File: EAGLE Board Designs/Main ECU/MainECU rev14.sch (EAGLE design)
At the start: 319 parts, among them J1 CONNECTOR-34__, J2 CONNECTOR-34__, J3 ADIS16460, K1 RELAY_DPDT_07DSMT, K2 RELAY_DPDT_07DSMT, K3 RELAY_DPDT_07DSMT, K4 RELAY_DPDT_07DSMT, K5 RELAY_DPDT_07DSMT, Q1 TRANSISTOR_N_MOS__DMG3406L-7, Q2 TRANSISTOR_P_MOS_SOT-23_DMP30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, Q3 TRANSISTOR_P_MOS_SOT-23_DMP30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, Q4 TRANSISTOR_N_MOS__DMG3406L-7, U1 MAX7400, U10 MCP3208, U11 MCP3208, U12 TCAN1051HQV-Q1, U13 TCAN1051HQV-Q1, U15 OPAMP_1_CHANNEL_OPA991, U16 LOGICGATE_OR, U17 OPAMP_1_CHANNEL_OPA991, U18 LOGICGATE_OR, U19 OPAMP_1_CHANNEL_OPA991, U2 MAX7400, U20 LOGICGATE_OR, U21 LOGICGATE_OR, U22 OPAMP_1_CHANNEL_OPA991, U23 LOGICGATE_NOR, U24 LOGICGATE_OR, U25 OPAMP_1_CHANNEL_OPA991, U26 OPAMP_1_CHANNEL_OPA991, U27 OPAMP_1_CHANNEL_OPA991, U28 LOGICGATE_AND_DCK3, U29 OPAMP_1_CHANNEL_OPA991, U3 MAX7400, U30 OPAMP_1_CHANNEL_OPA991, U31 TCAN1051HQV-Q1, U32 TCAN1051HQV-Q1, U33 TCAN1051HQV-Q1, U34 TCAN1051HQV-Q1, U35 MAX7400, U36 MAX7400, U37 ADM8316WBX30, U38 MAX7400, U4 MAX7400, U5 VOLTAGE_REGULATOR_SOT-223_3.3V, U6 MAX7400, U7 MAX7400, U8 MAX7400, U9 MAX7400

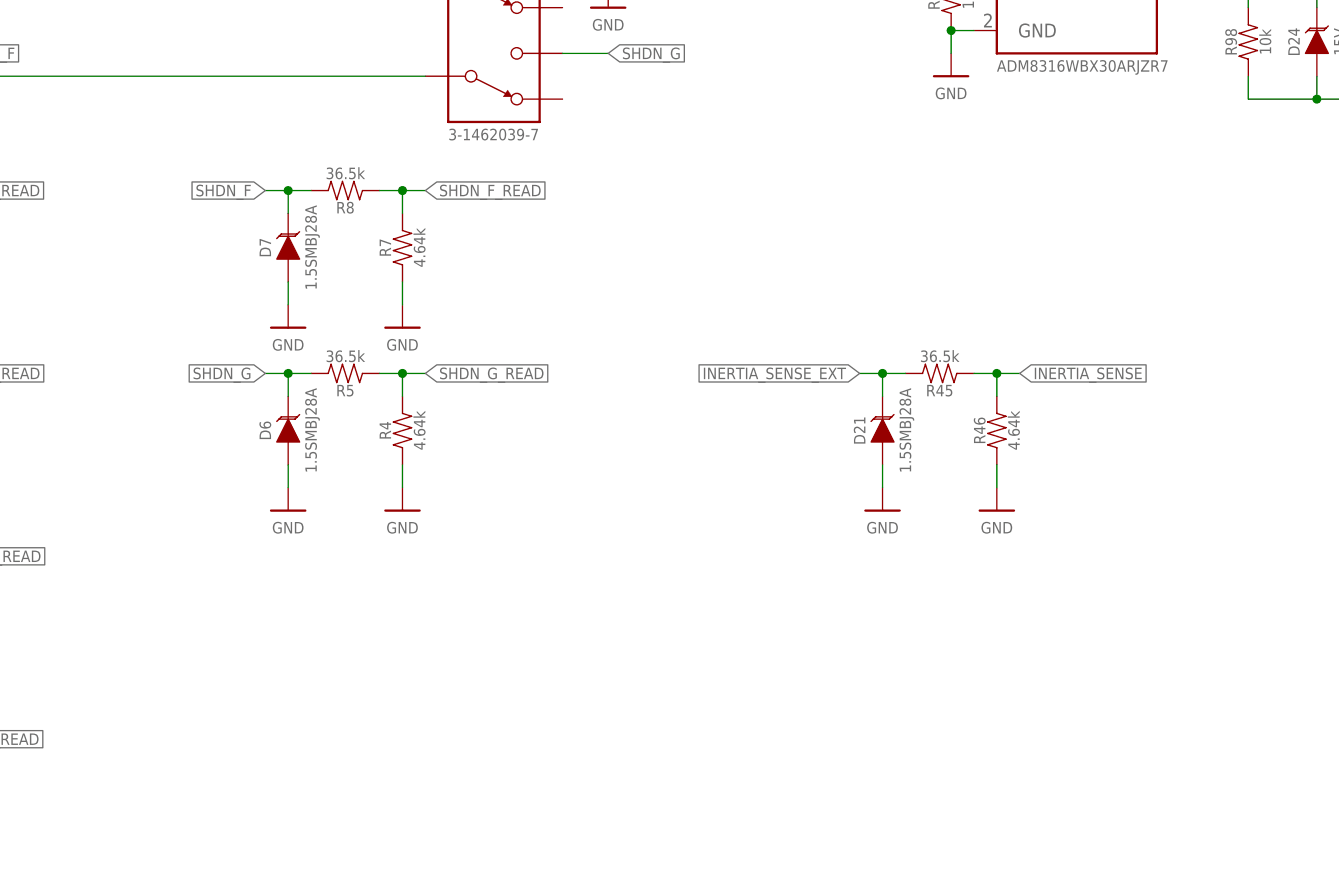
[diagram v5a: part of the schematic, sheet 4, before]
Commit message: added ECU->TCU serial, AMS&IMD sense
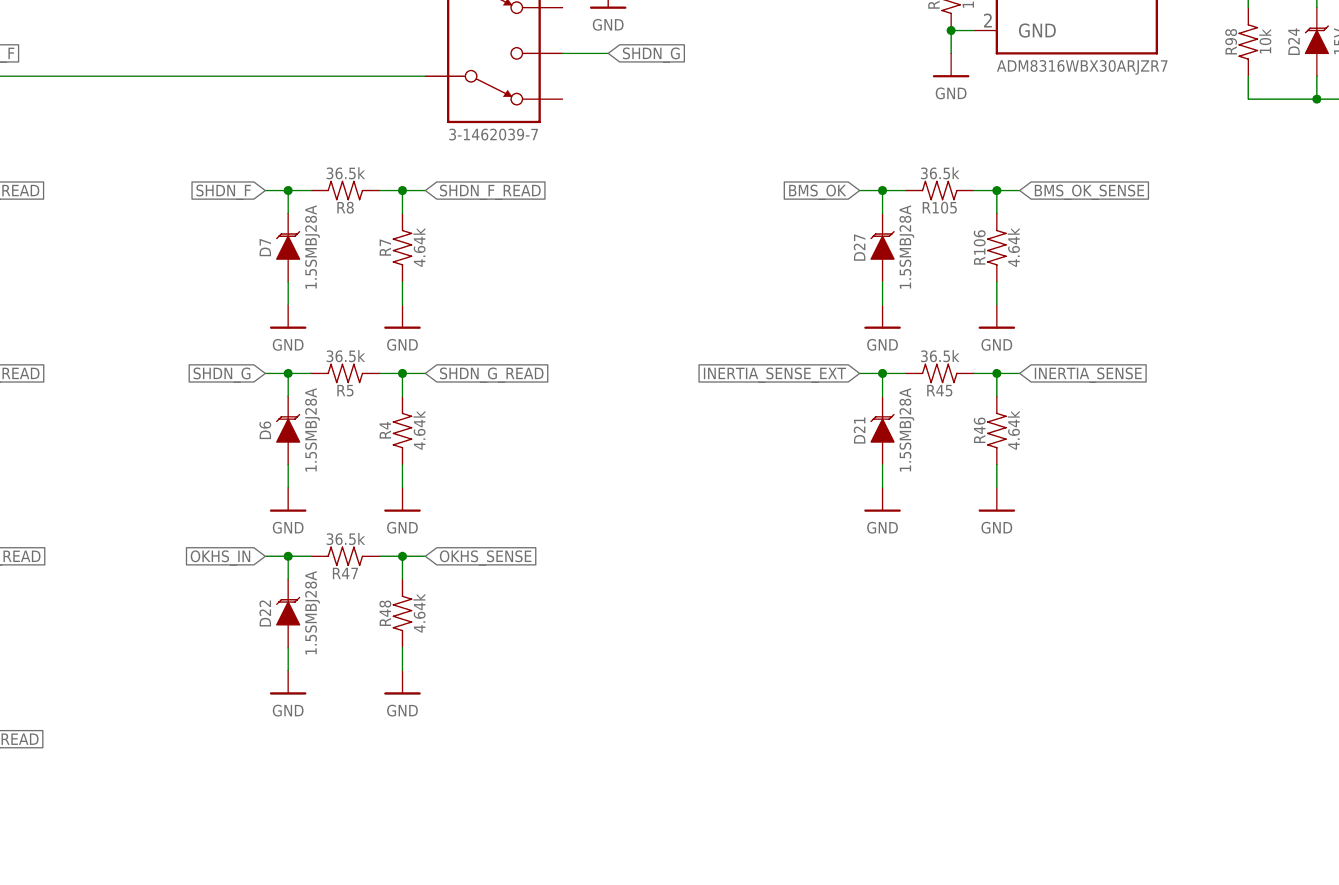
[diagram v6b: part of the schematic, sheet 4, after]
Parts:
- added D22, D27: TVS_DO-214AA_28V, HyTechDevices:TVS_DO-214AA_28V
- added R105, R47: RESISTOR_0603_36.5K, HyTechDevices:RESISTOR_0603_36.5K
- added R106, R48: RESISTOR_0603_4.64K, HyTechDevices:RESISTOR_0603_4.64K
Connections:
- removed net GPS_RX: A3.A0
- removed net GPS_TX: A3.A1
- new net BMS_OK_SENSE: A2.A2, R105.1, R106.2
- new net ECU_RX3: A2.A1, A3.A0
- new net ECU_TX3: A2.A0, A3.A1
- new net OKHS_SENSE: A2.A4, R47.1, R48.2
- net BMS_OK: now also D27.C, R105.2
- net GND: now also D22.A, D27.A, R106.1, R48.1
- net OKHS_IN: now also D22.C, R47.2
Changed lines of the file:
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@@
 <part name="P57" library="HyTechSupplies" deviceset="+3V3" device=""/>
 <part name="P58" library="HyTechSupplies" deviceset="+3V3" device=""/>
+<part name="R47" library="HyTechDevices" deviceset="RESISTOR_?_*" device="0603" technology="36.5K" value="RESISTOR_0603_36.5K"/>
+<part name="P59" library="HyTechSupplies" deviceset="GND" device=""/>
+<part name="R48" library="HyTechDevices" deviceset="RESISTOR_?_*" device="0603" technology="4.64K" value="RESISTOR_0603_4.64K"/>
+<part name="D22" library="HyTechDevices" deviceset="TVS_?_*" device="DO-214AA" technology="28V" value="TVS_DO-214AA_28V"/>
+<part name="P60" library="HyTechSupplies" deviceset="GND" device=""/>
+<part name="R105" library="HyTechDevices" deviceset="RESISTOR_?_*" device="0603" technology="36.5K" value="RESISTOR_0603_36.5K"/>
+<part name="P61" library="HyTechSupplies" deviceset="GND" device=""/>
+<part name="R106" library="HyTechDevices" deviceset="RESISTOR_?_*" device="0603" technology="4.64K" value="RESISTOR_0603_4.64K"/>
+<part name="D27" library="HyTechDevices" deviceset="TVS_?_*" device="DO-214AA" technology="28V" value="TVS_DO-214AA_28V"/>
+<part name="P63" library="HyTechSupplies" deviceset="GND" device=""/>
 </parts>
 <sheets>
@@
 <attribute name="VALUE" x="264.16" y="184.15" size="1.27" layer="96" align="top-center"/>
 </instance>
+<instance part="R47" gate="G$1" x="106.68" y="60.96" smashed="yes" rot="R180">
+<attribute name="NAME" x="107.95" y="59.69" size="1.27" layer="95" rot="R180" align="bottom-center"/>
+<attribute name="RESISTANCE" x="107.95" y="62.23" size="1.27" layer="96" rot="R180" align="top-center"/>
+</instance>
+<instance part="P59" gate="1" x="114.3" y="45.72" smashed="yes">
+<attribute name="VALUE" x="114.3" y="44.45" size="1.27" layer="96" align="top-center"/>
+</instance>
+<instance part="R48" gate="G$1" x="114.3" y="55.88" smashed="yes" rot="R90">
+<attribute name="NAME" x="113.03" y="54.61" size="1.27" layer="95" rot="R90" align="bottom-center"/>
+<attribute name="RESISTANCE" x="115.57" y="54.61" size="1.27" layer="96" rot="R90" align="top-center"/>
+</instance>
+<instance part="D22" gate="G$1" x="101.6" y="55.88" smashed="yes" rot="R90">
+<attribute name="NAME" x="99.695" y="54.61" size="1.27" layer="95" rot="R90" align="bottom-center"/>
+<attribute name="MPN" x="103.505" y="54.61" size="1.27" layer="96" rot="R90" align="top-center"/>
+</instance>
+<instance part="P60" gate="1" x="101.6" y="45.72" smashed="yes">
+<attribute name="VALUE" x="101.6" y="44.45" size="1.27" layer="96" align="top-center"/>
+</instance>
+<instance part="R105" gate="G$1" x="172.72" y="101.6" smashed="yes" rot="R180">
+<attribute name="NAME" x="173.99" y="100.33" size="1.27" layer="95" rot="R180" align="bottom-center"/>
+<attribute name="RESISTANCE" x="173.99" y="102.87" size="1.27" layer="96" rot="R180" align="top-center"/>
+</instance>
+<instance part="P61" gate="1" x="180.34" y="86.36" smashed="yes">
+<attribute name="VALUE" x="180.34" y="85.09" size="1.27" layer="96" align="top-center"/>
+</instance>
+<instance part="R106" gate="G$1" x="180.34" y="96.52" smashed="yes" rot="R90">
+<attribute name="NAME" x="179.07" y="95.25" size="1.27" layer="95" rot="R90" align="bottom-center"/>
+<attribute name="RESISTANCE" x="181.61" y="95.25" size="1.27" layer="96" rot="R90" align="top-center"/>
+</instance>
+<instance part="D27" gate="G$1" x="167.64" y="96.52" smashed="yes" rot="R90">
+<attribute name="NAME" x="165.735" y="95.25" size="1.27" layer="95" rot="R90" align="bottom-center"/>
+<attribute name="MPN" x="169.545" y="95.25" size="1.27" layer="96" rot="R90" align="top-center"/>
+</instance>
+<instance part="P63" gate="1" x="167.64" y="86.36" smashed="yes">
+<attribute name="VALUE" x="167.64" y="85.09" size="1.27" layer="96" align="top-center"/>
+</instance>
 </instances>
 <busses>
@@
 <label x="63.5" y="190.5" size="1.27" layer="95" xref="yes"/>
 </segment>
+<segment>
+<label x="99.06" y="60.96" size="1.27" layer="95" rot="R180" xref="yes"/>
+<pinref part="R47" gate="G$1" pin="2"/>
+<wire x1="104.14" y1="60.96" x2="101.6" y2="60.96" width="0.1524" layer="91"/>
+<pinref part="D22" gate="G$1" pin="C"/>
+<wire x1="101.6" y1="60.96" x2="99.06" y2="60.96" width="0.1524" layer="91"/>
+<wire x1="101.6" y1="58.42" x2="101.6" y2="60.96" width="0.1524" layer="91"/>
+<junction x="101.6" y="60.96"/>
+</segment>
 </net>
 <net name="LATCH_BTN" class="0">
@@
 <wire x1="264.16" y1="190.5" x2="264.16" y2="187.96" width="0.1524" layer="91"/>
 </segment>
+<segment>
+<pinref part="P59" gate="1" pin="GND"/>
+<pinref part="R48" gate="G$1" pin="1"/>
+<wire x1="114.3" y1="50.8" x2="114.3" y2="48.26" width="0.1524" layer="91"/>
+</segment>
+<segment>
+<pinref part="D22" gate="G$1" pin="A"/>
+<pinref part="P60" gate="1" pin="GND"/>
+<wire x1="101.6" y1="50.8" x2="101.6" y2="48.26" width="0.1524" layer="91"/>
+</segment>
+<segment>
+<pinref part="P61" gate="1" pin="GND"/>
+<pinref part="R106" gate="G$1" pin="1"/>
+<wire x1="180.34" y1="91.44" x2="180.34" y2="88.9" width="0.1524" layer="91"/>
+</segment>
+<segment>
+<pinref part="D27" gate="G$1" pin="A"/>
+<pinref part="P63" gate="1" pin="GND"/>
+<wire x1="167.64" y1="91.44" x2="167.64" y2="88.9" width="0.1524" layer="91"/>
+</segment>
 </net>
 <net name="SHDN_B" class="0">
@@
 <label x="137.16" y="190.5" size="1.27" layer="95" xref="yes"/>
 </segment>
+<segment>
+<label x="165.1" y="101.6" size="1.27" layer="95" rot="R180" xref="yes"/>
+<pinref part="R105" gate="G$1" pin="2"/>
+<wire x1="170.18" y1="101.6" x2="167.64" y2="101.6" width="0.1524" layer="91"/>
+<pinref part="D27" gate="G$1" pin="C"/>
+<wire x1="167.64" y1="101.6" x2="165.1" y2="101.6" width="0.1524" layer="91"/>
+<wire x1="167.64" y1="99.06" x2="167.64" y2="101.6" width="0.1524" layer="91"/>
+<junction x="167.64" y="101.6"/>
+</segment>
 </net>
 <net name="BSPD_OK" class="0">
@@
 </segment>
 </net>
+<net name="BMS_OK_SENSE" class="0">
+<segment>
+<pinref part="R105" gate="G$1" pin="1"/>
+<label x="182.88" y="101.6" size="1.27" layer="95" xref="yes"/>
+<wire x1="177.8" y1="101.6" x2="180.34" y2="101.6" width="0.1524" layer="91"/>
+<wire x1="180.34" y1="101.6" x2="182.88" y2="101.6" width="0.1524" layer="91"/>
+<pinref part="R106" gate="G$1" pin="2"/>
+<wire x1="180.34" y1="99.06" x2="180.34" y2="101.6" width="0.1524" layer="91"/>
+<junction x="180.34" y="101.6"/>
+</segment>
+</net>
+<net name="OKHS_SENSE" class="0">
+<segment>
+<pinref part="R47" gate="G$1" pin="1"/>
+<label x="116.84" y="60.96" size="1.27" layer="95" xref="yes"/>
+<wire x1="111.76" y1="60.96" x2="114.3" y2="60.96" width="0.1524" layer="91"/>
+<wire x1="114.3" y1="60.96" x2="116.84" y2="60.96" width="0.1524" layer="91"/>
+<pinref part="R48" gate="G$1" pin="2"/>
+<wire x1="114.3" y1="58.42" x2="114.3" y2="60.96" width="0.1524" layer="91"/>
+<junction x="114.3" y="60.96"/>
+</segment>
+</net>
 </nets>
 </sheet>
@@
 </segment>
 </net>
+<net name="ECU_TX3" class="0">
+<segment>
+<pinref part="A2" gate="G$1" pin="A0"/>
+<wire x1="208.28" y1="104.14" x2="200.66" y2="104.14" width="0.1524" layer="91"/>
+<label x="200.66" y="104.14" size="1.27" layer="95" rot="R180" xref="yes"/>
+</segment>
+</net>
+<net name="ECU_RX3" class="0">
+<segment>
+<pinref part="A2" gate="G$1" pin="A1"/>
+<wire x1="208.28" y1="101.6" x2="200.66" y2="101.6" width="0.1524" layer="91"/>
+<label x="200.66" y="101.6" size="1.27" layer="95" rot="R180" xref="yes"/>
+</segment>
+</net>
+<net name="OKHS_SENSE" class="0">
+<segment>
+<pinref part="A2" gate="G$1" pin="A4"/>
+<wire x1="208.28" y1="93.98" x2="200.66" y2="93.98" width="0.1524" layer="91"/>
+<label x="200.66" y="93.98" size="1.27" layer="95" rot="R180" xref="yes"/>
+</segment>
+</net>
+<net name="BMS_OK_SENSE" class="0">
+<segment>
+<pinref part="A2" gate="G$1" pin="A2"/>
+<wire x1="208.28" y1="99.06" x2="200.66" y2="99.06" width="0.1524" layer="91"/>
+<label x="200.66" y="99.06" size="1.27" layer="95" rot="R180" xref="yes"/>
+</segment>
+</net>
 </nets>
 </sheet>
@@
 <text x="38.1" y="175.26" size="1.778" layer="97">Data Acq</text>
 <text x="78.74" y="111.76" size="1.27" layer="97">Serial2</text>
-<text x="10.16" y="119.38" size="1.27" layer="97">Serial3</text>
+<text x="7.62" y="119.38" size="1.27" layer="97">Serial3</text>
 <text x="78.74" y="152.4" size="1.27" layer="97">Serial8</text>
 </plain>
@@
 </segment>
 </net>
-<net name="GPS_RX" class="0">
-<segment>
-<pinref part="A3" gate="G$1" pin="A0"/>
-<wire x1="35.56" y1="121.92" x2="27.94" y2="121.92" width="0.1524" layer="91"/>
-<label x="27.94" y="121.92" size="1.27" layer="95" rot="R180" xref="yes"/>
-</segment>
-</net>
-<net name="GPS_TX" class="0">
-<segment>
-<pinref part="A3" gate="G$1" pin="A1"/>
-<wire x1="35.56" y1="119.38" x2="27.94" y2="119.38" width="0.1524" layer="91"/>
-<label x="27.94" y="119.38" size="1.27" layer="95" rot="R180" xref="yes"/>
-</segment>
-</net>
 <net name="GPS_FIX" class="0">
 <segment>
@@
 </segment>
 </net>
+<net name="ECU_TX3" class="0">
+<segment>
+<pinref part="A3" gate="G$1" pin="A1"/>
+<wire x1="35.56" y1="119.38" x2="27.94" y2="119.38" width="0.1524" layer="91"/>
+<label x="27.94" y="119.38" size="1.27" layer="95" rot="R180" xref="yes"/>
+</segment>
+</net>
+<net name="ECU_RX3" class="0">
+<segment>
+<pinref part="A3" gate="G$1" pin="A0"/>
+<wire x1="35.56" y1="121.92" x2="27.94" y2="121.92" width="0.1524" layer="91"/>
+<label x="27.94" y="121.92" size="1.27" layer="95" rot="R180" xref="yes"/>
+</segment>
+</net>
